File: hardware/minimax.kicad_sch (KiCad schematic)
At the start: 5 parts, among them J1 DF37NC-30DS-0.4V_51_, U1 MAX96717GTJ/VY+

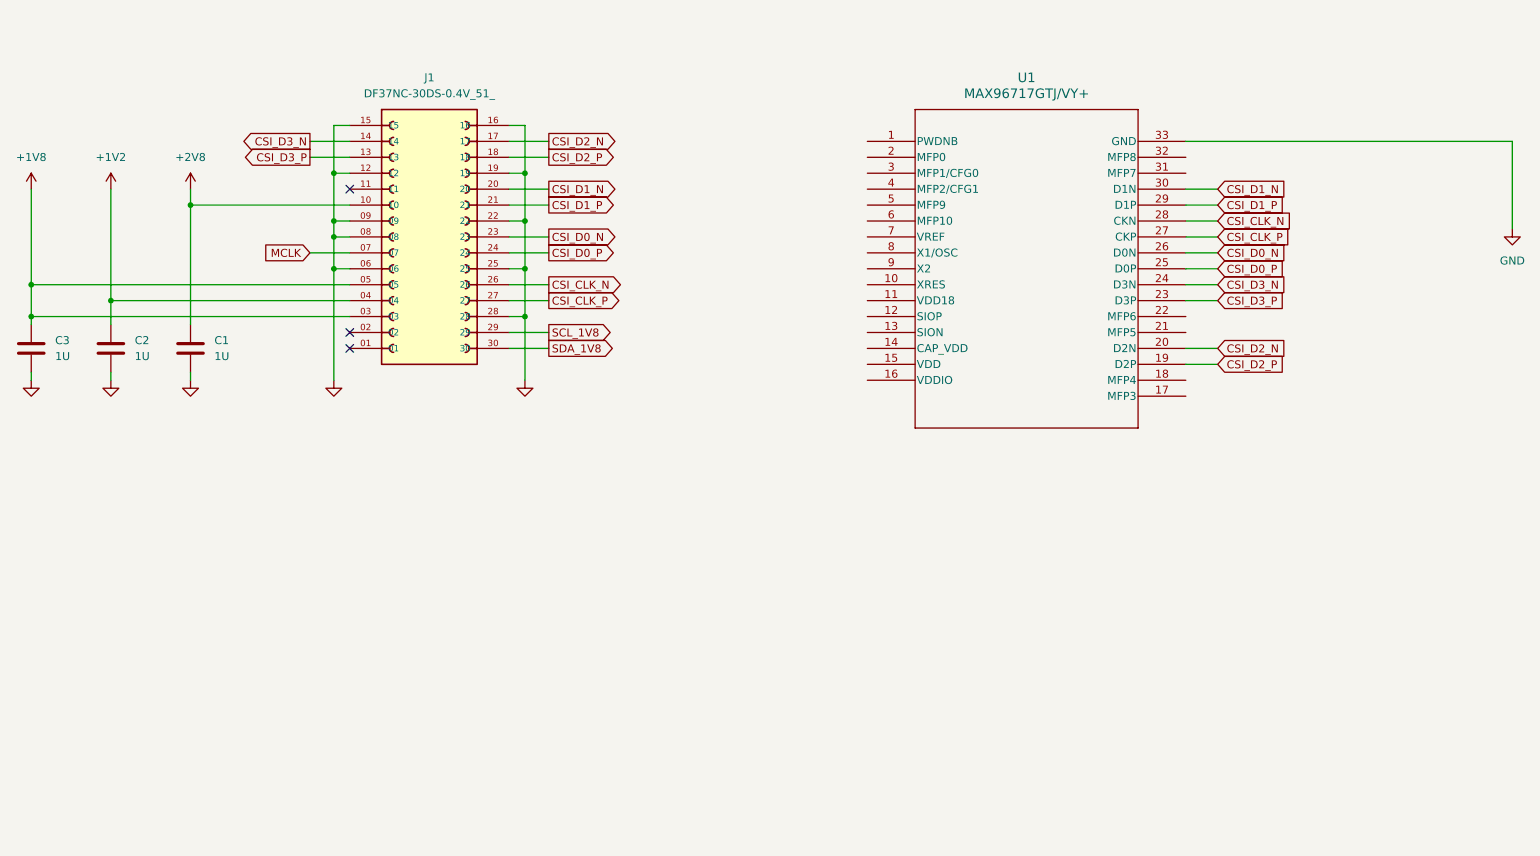
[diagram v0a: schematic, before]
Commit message: mipi interface land swapping
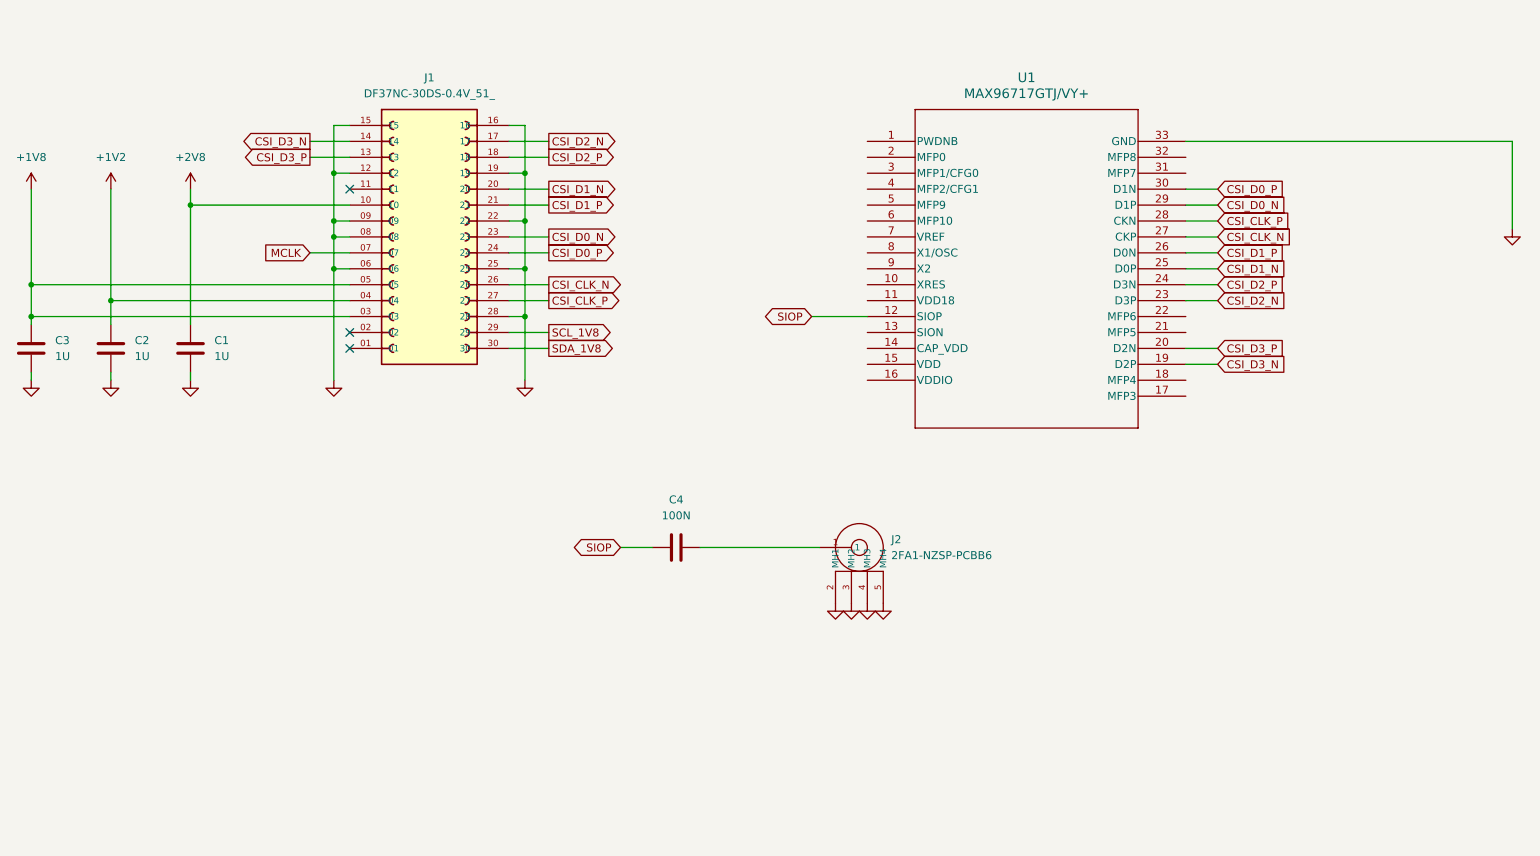
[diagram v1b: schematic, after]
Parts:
- added C4: 100N, Capacitor_SMD:C_0402_1005Metric, symbol Device:C
- added J2: 2FA1-NZSP-PCBB6, user:2FA1-NZSP-PCBB6, symbol user:2FA1-NZSP-PCBB6
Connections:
- net CSI_CLK_N: now also U1.27 (CKP); no longer U1.28 (CKN)
- net CSI_CLK_P: now also U1.28 (CKN); no longer U1.27 (CKP)
- net CSI_D0_N: now also U1.29 (D1P); no longer U1.26 (D0N)
- net CSI_D0_P: now also U1.30 (D1N); no longer U1.25 (D0P)
- net CSI_D1_N: now also U1.25 (D0P); no longer U1.30 (D1N)
- net CSI_D1_P: now also U1.26 (D0N); no longer U1.29 (D1P)
- net CSI_D2_N: now also U1.23 (D3P); no longer U1.20 (D2N)
- net CSI_D2_P: now also U1.24 (D3N); no longer U1.19 (D2P)
- net CSI_D3_N: now also U1.19 (D2P); no longer U1.24 (D3N)
- net CSI_D3_P: now also U1.20 (D2N); no longer U1.23 (D3P)
- net GND: now also J2.2 (MH1), J2.3 (MH2), J2.4 (MH3), J2.5 (MH4)
- net SIOP: now reaches U1.12 (SIOP)
- net SIOP: now also C4.1
- new net: C4.2, J2.1

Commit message: cleaned schematics and moving to rpi v2 camera form factor
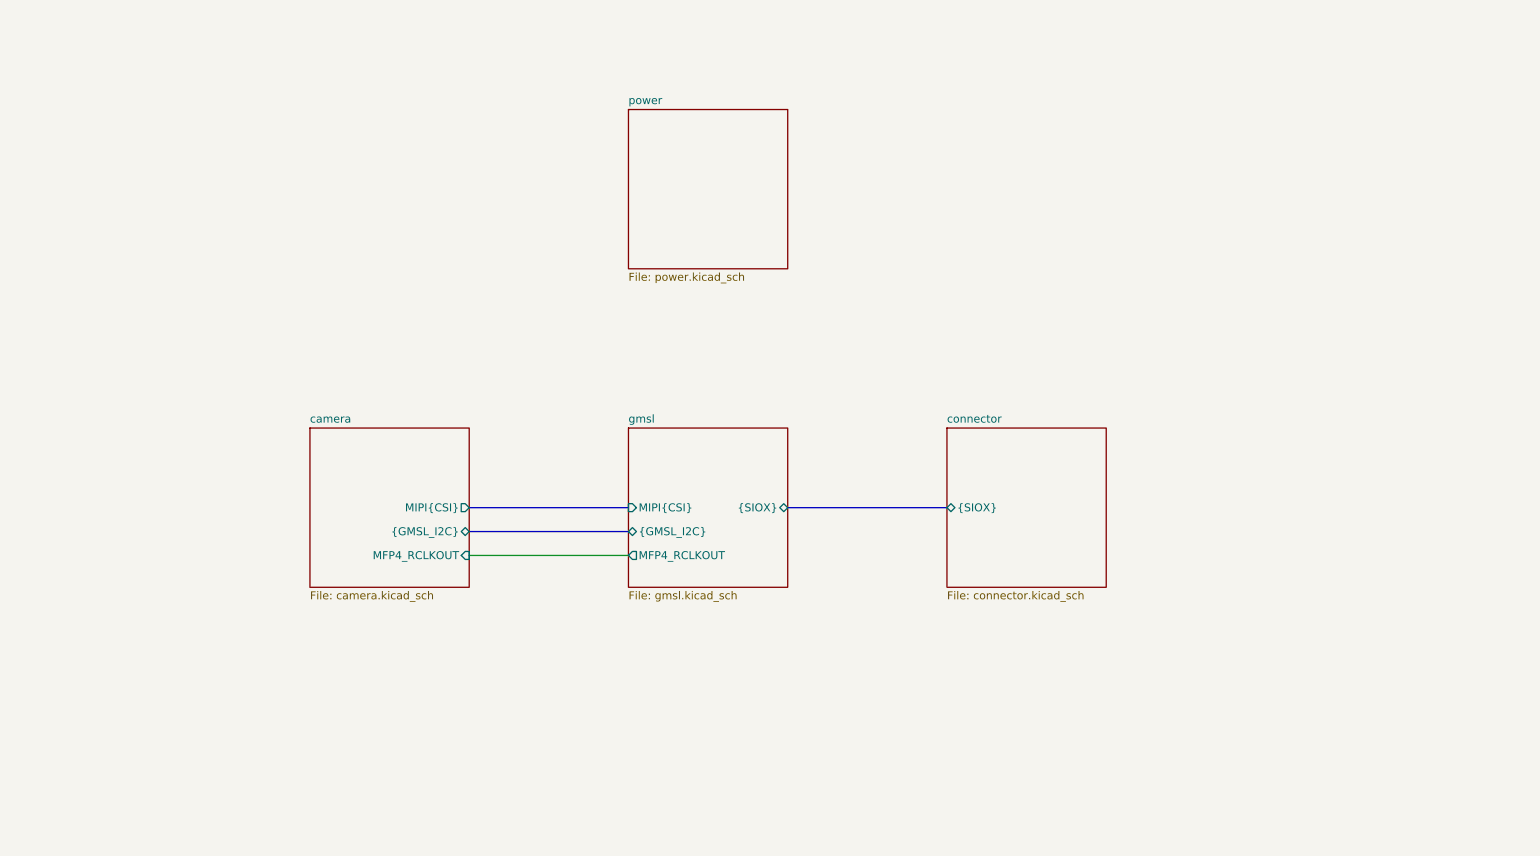
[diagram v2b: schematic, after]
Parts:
- removed C1, C2, C3: 1U, Capacitor_SMD:C_0402_1005Metric, symbol Device:C
- removed C4: 100N, Capacitor_SMD:C_0402_1005Metric, symbol Device:C
- removed J1: DF37NC-30DS-0.4V_51_, user:HRS_DF37NC-30DS-0.4V_51_, symbol user:DF37NC-30DS-0.4V_51_
- removed J2: 2FA1-NZSP-PCBB6, user:2FA1-NZSP-PCBB6, symbol user:2FA1-NZSP-PCBB6
- removed U1: MAX96717GTJ/VY+, user:ADI_21-100156_T3255Y-8, symbol user:MAX96717GTJ_VY+
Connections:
- no-connect marks 3 -> 0
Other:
- added sheet camera (camera.kicad_sch)
- added sheet connector (connector.kicad_sch)
- added sheet gmsl (gmsl.kicad_sch)
- added sheet power (power.kicad_sch)

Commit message: cleaned up serializer with comments and project hierarchy
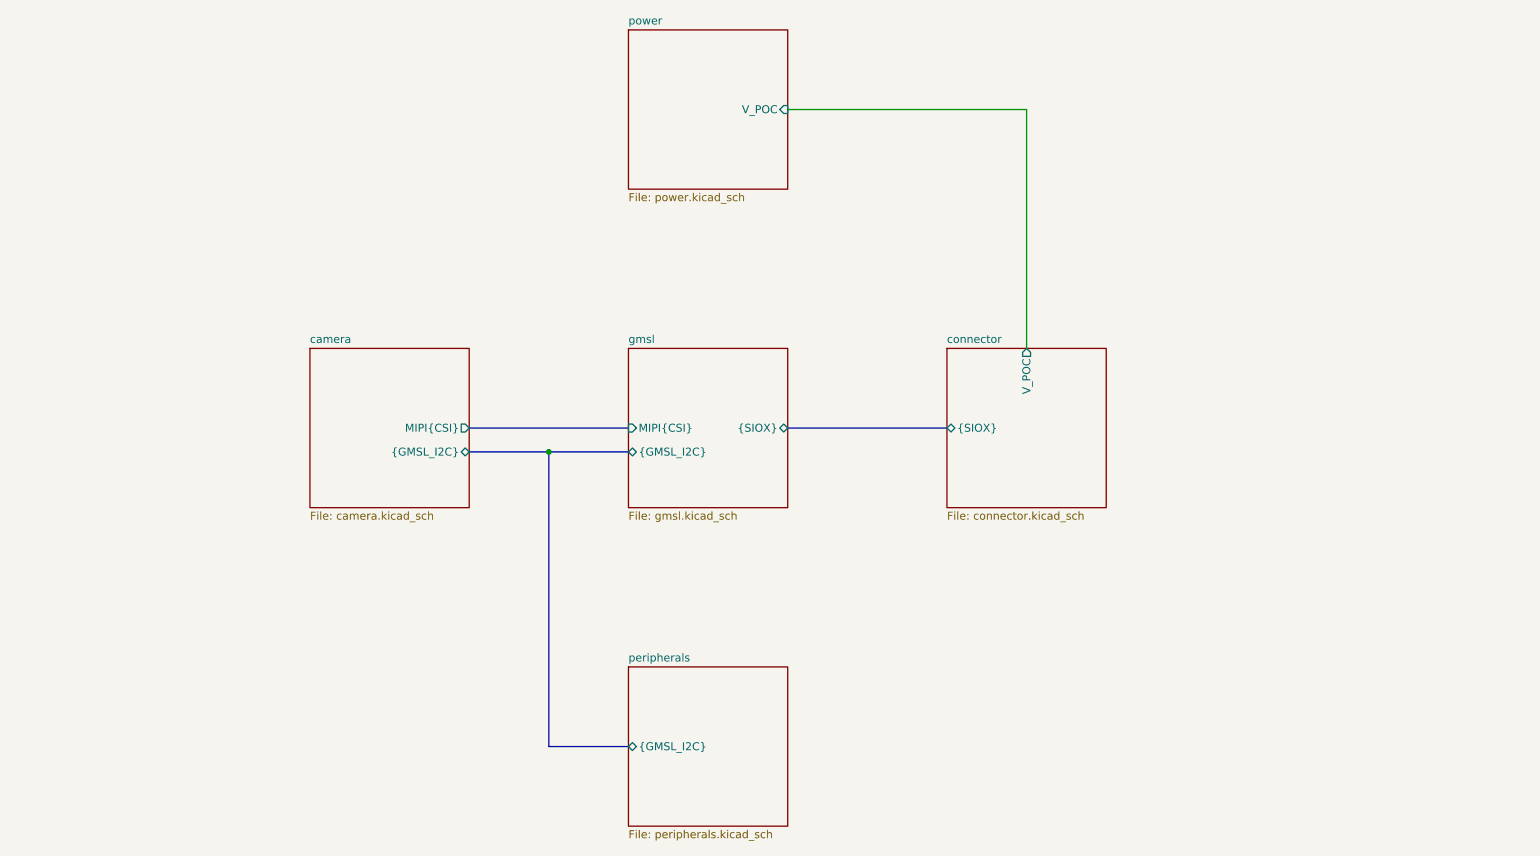
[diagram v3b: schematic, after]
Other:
- added sheet peripherals (peripherals.kicad_sch)
- sheet camera ports: added none; removed MFP4_RCLKOUT
- sheet connector ports: added V_POC; removed none
- sheet gmsl ports: added none; removed MFP4_RCLKOUT
- sheet power ports: added V_POC; removed none
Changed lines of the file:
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@@
 	(generator_version "8.0")
 	(paper "A4")
+	(junction
+		(at 114.3 105.41)
+		(diameter 0)
+		(color 0 0 0 0)
+	)
+	(bus
+		(pts
+			(xy 114.3 105.41) (xy 127 105.41)
+		)
+		(stroke
+			(width 0)
+			(type default)
+		)
+	)
+	(bus
+		(pts
+			(xy 101.6 105.41) (xy 114.3 105.41)
+		)
+		(stroke
+			(width 0)
+			(type default)
+		)
+	)
+	(bus
+		(pts
+			(xy 114.3 152.4) (xy 114.3 105.41)
+		)
+		(stroke
+			(width 0)
+			(type default)
+		)
+	)
+	(bus
+		(pts
+			(xy 101.6 101.6) (xy 127 101.6)
+		)
+		(stroke
+			(width 0)
+			(type default)
+		)
+	)
+	(bus
+		(pts
+			(xy 127 152.4) (xy 114.3 152.4)
+		)
+		(stroke
+			(width 0)
+			(type default)
+		)
+	)
 	(wire
 		(pts
-			(xy 101.6 121.92) (xy 127 121.92)
-		)
-		(stroke
-			(width 0)
-			(type default)
-		)
-	)
-	(bus
-		(pts
-			(xy 101.6 118.11) (xy 127 118.11)
-		)
-		(stroke
-			(width 0)
-			(type default)
-		)
-	)
-	(bus
-		(pts
-			(xy 101.6 114.3) (xy 127 114.3)
-		)
-		(stroke
-			(width 0)
-			(type default)
-		)
-	)
-	(bus
-		(pts
-			(xy 152.4 114.3) (xy 177.8 114.3)
-		)
-		(stroke
-			(width 0)
-			(type default)
-		)
-	)
-	(sheet
-		(at 127 101.6)
+			(xy 190.5 88.9) (xy 190.5 50.8)
+		)
+		(stroke
+			(width 0)
+			(type default)
+		)
+	)
+	(bus
+		(pts
+			(xy 152.4 101.6) (xy 177.8 101.6)
+		)
+		(stroke
+			(width 0)
+			(type default)
+		)
+	)
+	(wire
+		(pts
+			(xy 190.5 50.8) (xy 152.4 50.8)
+		)
+		(stroke
+			(width 0)
+			(type default)
+		)
+	)
+	(sheet
+		(at 127 139.7)
+		(size 25.4 25.4)
+		(fields_autoplaced yes)
+		(stroke
+			(width 0.1524)
+			(type solid)
+		)
+		(fill
+			(color 0 0 0 0.0000)
+		)
+		(property "Sheetname" "peripherals"
+			(at 127 138.9884 0)
+			(effects
+				(font
+					(size 1.27 1.27)
+				)
+				(justify left bottom)
+			)
+		)
+		(property "Sheetfile" "peripherals.kicad_sch"
+			(at 127 165.6846 0)
+			(effects
+				(font
+					(size 1.27 1.27)
+				)
+				(justify left top)
+			)
+		)
+		(pin "{GMSL_I2C}" bidirectional
+			(at 127 152.4 180)
+			(effects
+				(font
+					(size 1.27 1.27)
+				)
+				(justify left)
+			)
+		)
+		(instances
+			(project "minimax"
+				(path "/d9b03904-3e0d-40cc-bc70-bbd63756773a"
+					(page "6")
+				)
+			)
+		)
+	)
+	(sheet
+		(at 127 88.9)
 		(size 25.4 25.4)
 		(fields_autoplaced yes)
@@
 		)
 		(property "Sheetname" "gmsl"
-			(at 127 100.8884 0)
+			(at 127 88.1884 0)
 			(effects
 				(font
@@
 		)
 		(property "Sheetfile" "gmsl.kicad_sch"
-			(at 127 127.5846 0)
+			(at 127 114.8846 0)
 			(effects
 				(font
@@
 		)
 		(pin "MIPI{CSI}" input
-			(at 127 114.3 180)
+			(at 127 101.6 180)
 			(effects
 				(font
@@
 			)
 		)
-		(pin "MFP4_RCLKOUT" output
-			(at 127 121.92 180)
+		(pin "{GMSL_I2C}" bidirectional
+			(at 127 105.41 180)
 			(effects
 				(font
@@
 			)
 		)
-		(pin "{GMSL_I2C}" bidirectional
-			(at 127 118.11 180)
-			(effects
-				(font
-					(size 1.27 1.27)
-				)
-				(justify left)
-			)
-		)
 		(pin "{SIOX}" bidirectional
-			(at 152.4 114.3 0)
+			(at 152.4 101.6 0)
 			(effects
 				(font
@@
 	)
 	(sheet
-		(at 177.8 101.6)
+		(at 177.8 88.9)
 		(size 25.4 25.4)
 		(fields_autoplaced yes)
@@
 		)
 		(property "Sheetname" "connector"
-			(at 177.8 100.8884 0)
+			(at 177.8 88.1884 0)
 			(effects
 				(font
@@
 		)
 		(property "Sheetfile" "connector.kicad_sch"
-			(at 177.8 127.5846 0)
+			(at 177.8 114.8846 0)
 			(effects
 				(font
@@
 		)
 		(pin "{SIOX}" bidirectional
-			(at 177.8 114.3 180)
+			(at 177.8 101.6 180)
 			(effects
 				(font
@@
 				)
 				(justify left)
+			)
+		)
+		(pin "V_POC" output
+			(at 190.5 88.9 90)
+			(effects
+				(font
+					(size 1.27 1.27)
+				)
+				(justify right)
 			)
 		)
@@
 	)
 	(sheet
-		(at 76.2 101.6)
+		(at 76.2 88.9)
 		(size 25.4 25.4)
 		(fields_autoplaced yes)
@@
 		)
 		(property "Sheetname" "camera"
-			(at 76.2 100.8884 0)
+			(at 76.2 88.1884 0)
 			(effects
 				(font
@@
 		)
 		(property "Sheetfile" "camera.kicad_sch"
-			(at 76.2 127.5846 0)
+			(at 76.2 114.8846 0)
 			(effects
 				(font
@@
 		)
 		(pin "MIPI{CSI}" output
-			(at 101.6 114.3 0)
+			(at 101.6 101.6 0)
 			(effects
 				(font
@@
 		)
 		(pin "{GMSL_I2C}" bidirectional
-			(at 101.6 118.11 0)
-			(effects
-				(font
-					(size 1.27 1.27)
-				)
-				(justify right)
-			)
-		)
-		(pin "MFP4_RCLKOUT" input
-			(at 101.6 121.92 0)
+			(at 101.6 105.41 0)
 			(effects
 				(font
@@
 	)
 	(sheet
-		(at 127 50.8)
+		(at 127 38.1)
 		(size 25.4 25.4)
 		(fields_autoplaced yes)
@@
 		)
 		(property "Sheetname" "power"
-			(at 127 50.0884 0)
+			(at 127 37.3884 0)
 			(effects
 				(font
@@
 		)
 		(property "Sheetfile" "power.kicad_sch"
-			(at 127 76.7846 0)
-			(effects
-				(font
-					(size 1.27 1.27)
-				)
-				(justify left top)
-			)
-		)
+			(at 127 64.0846 0)
+			(effects
+				(font
+					(size 1.27 1.27)
+				)
+				(justify left top)
+			)
+		)
+		(pin "V_POC" input
+			(at 152.4 50.8 0)
+			(effects
+				(font
+					(size 1.27 1.27)
+				)
+				(justify right)
+			)
+		)

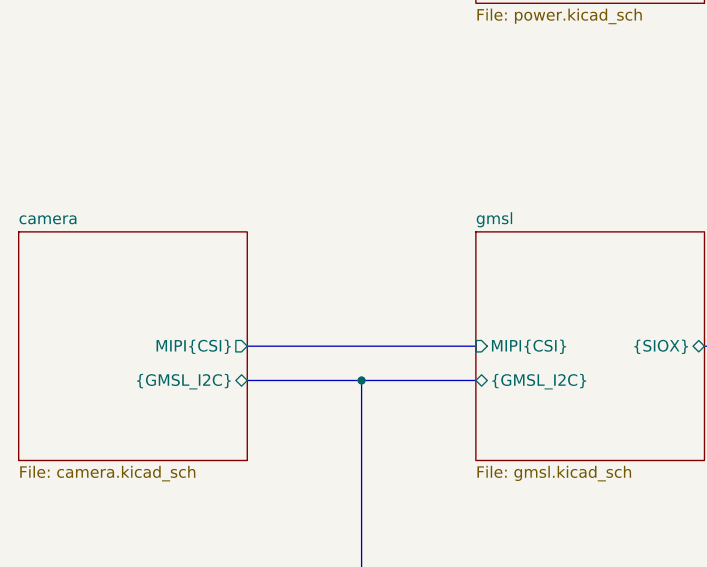
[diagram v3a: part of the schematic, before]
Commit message: started power, added smt fakra
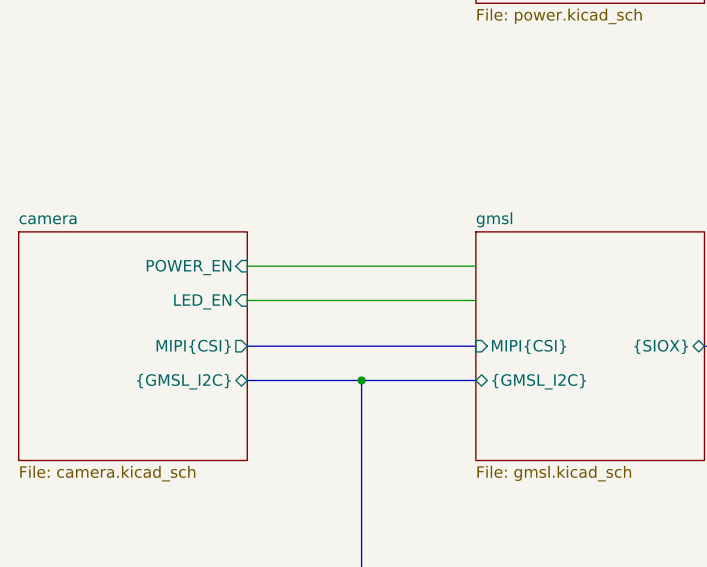
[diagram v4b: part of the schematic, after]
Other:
- sheet camera ports: added LED_EN, POWER_EN; removed none
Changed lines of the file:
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@@
 		(color 0 0 0 0)
 	)
+	(wire
+		(pts
+			(xy 101.6 92.71) (xy 127 92.71)
+		)
+		(stroke
+			(width 0)
+			(type default)
+		)
+	)
 	(bus
 		(pts
@@
 		(pts
 			(xy 152.4 101.6) (xy 177.8 101.6)
+		)
+		(stroke
+			(width 0)
+			(type default)
+		)
+	)
+	(wire
+		(pts
+			(xy 101.6 96.52) (xy 127 96.52)
 		)
 		(stroke
@@
 			(effects
 				(font
+					(size 1.27 1.27)
+				)
+				(justify right)
+			)
+		)
+		(pin "POWER_EN" input
+			(at 101.6 92.71 0)
+			(effects
+				(font
+					(size 1.27 1.27)
+				)
+				(justify right)
+			)
+		)
+		(pin "LED_EN" input
+			(at 101.6 96.52 0)
+			(effects
+				(font
